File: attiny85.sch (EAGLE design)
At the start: 8 parts, among them U1 TINY85-20-DIP

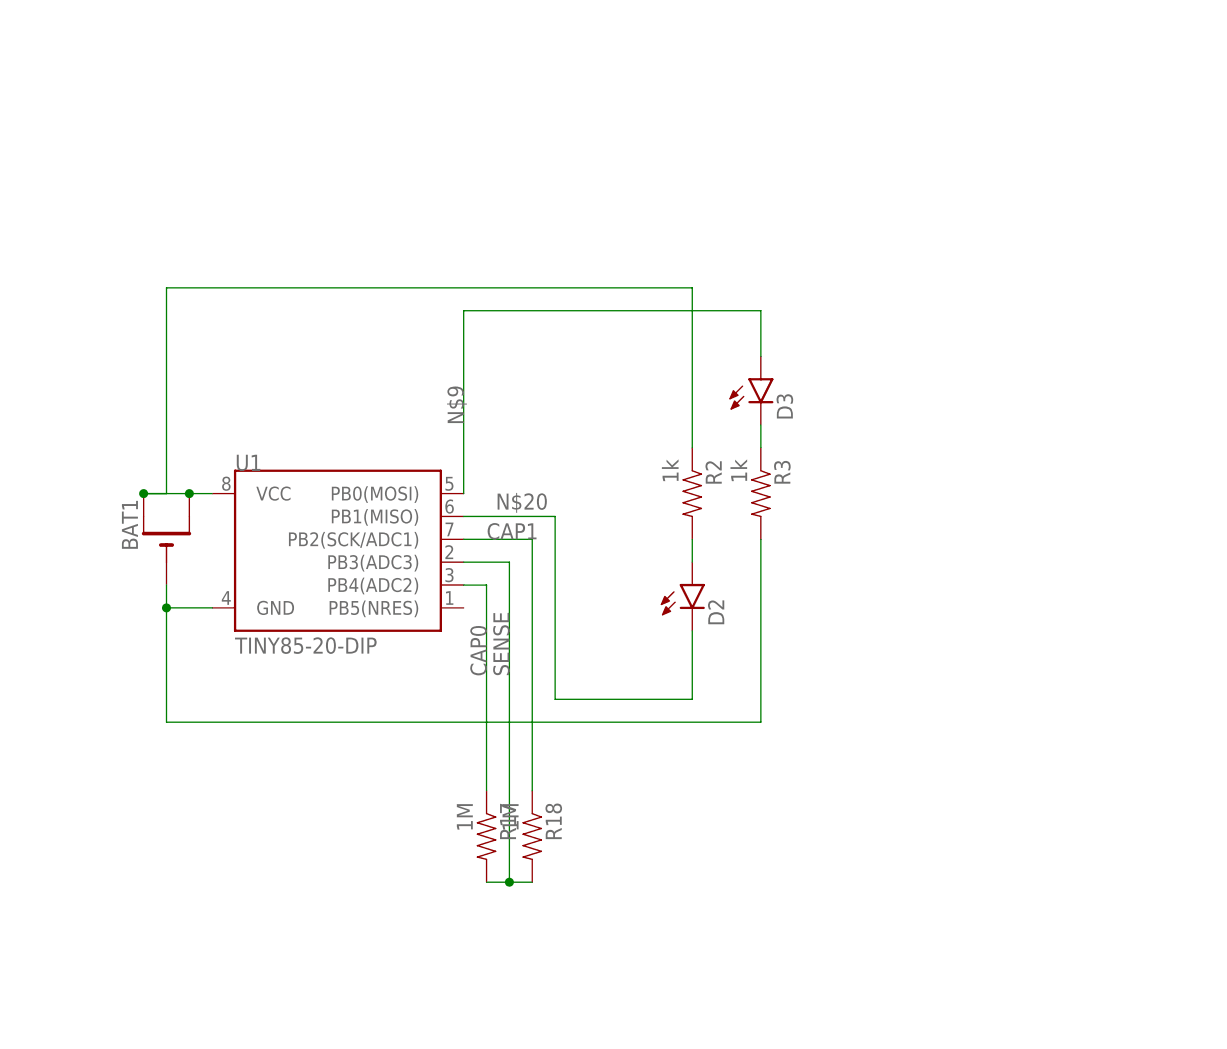
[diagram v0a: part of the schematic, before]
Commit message: Updated schematic and layout for surface mount components
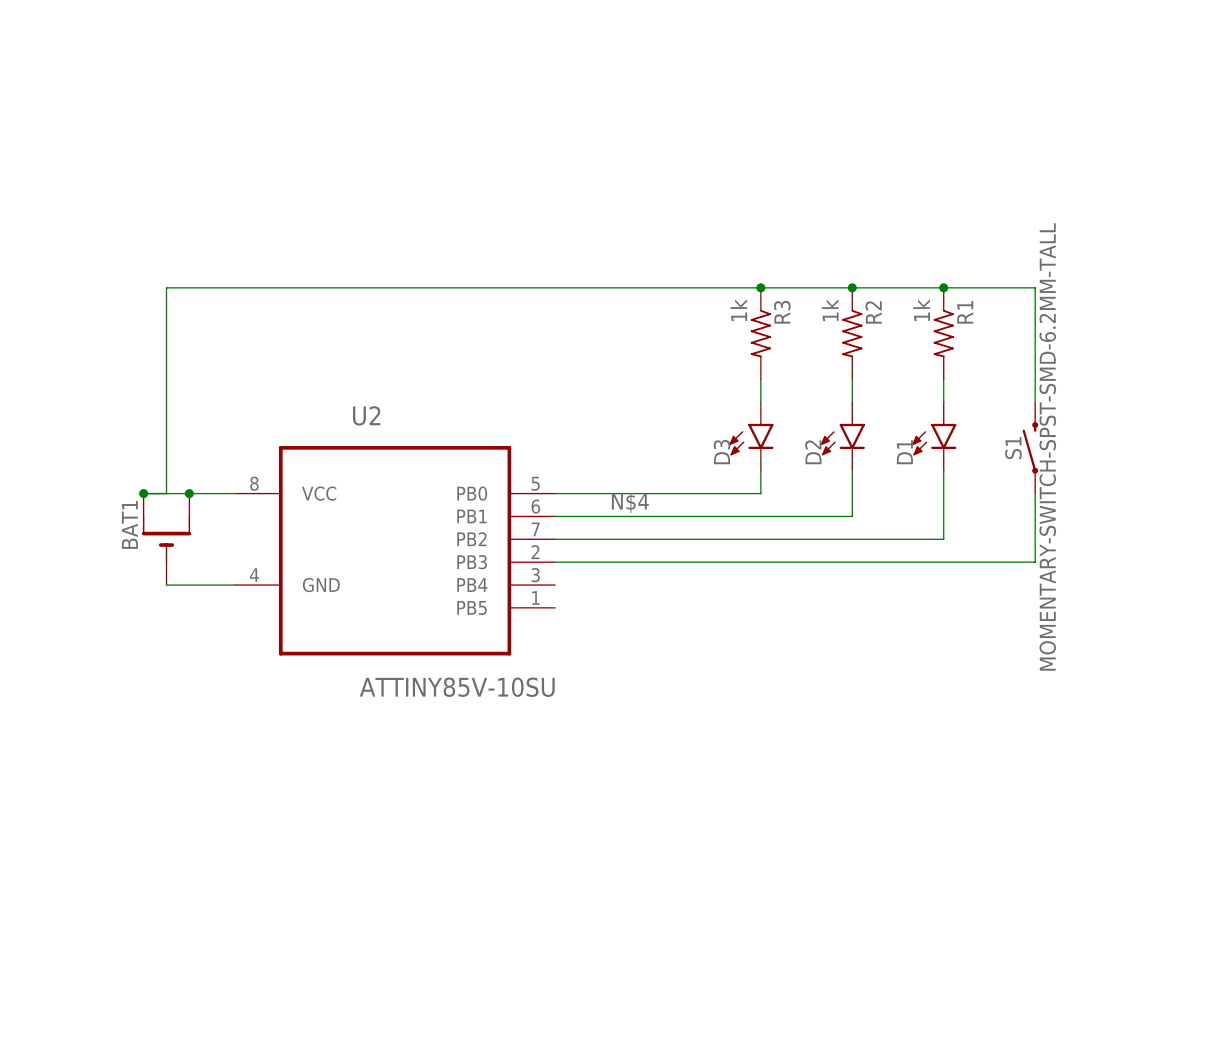
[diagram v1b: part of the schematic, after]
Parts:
- removed R17, R18: 1M, SparkFun-Resistors:1KOHM-1/4W-5%(PTH)
- removed U1: TINY85-20-DIP, SparkFun-DigitalIC:ATTINY45TINY85-20-DIP
- added D1: (no value), SparkFun-LED:LED1206
- added R1: 1k, adafruit:R-US_M1206
- added S1: MOMENTARY-SWITCH-SPST-SMD-6.2MM-TALL, SparkFun-Switches:MOMENTARY-SWITCH-SPST-SMD-6.2MM-TALL
- added U2: ATTINY85V-10SU, Atmel_By_element14_Batch_1-00:ATTINY85V-10SU
- BAT1: device adafruit:CR2032THM -> adafruit:CR2032SMT
- D2, D3: device LED:LED5MM -> SparkFun-LED:LED1206
- R2, R3: device SparkFun-Resistors:1KOHM-1/4W-5%(PTH) -> adafruit:R-US_M1206
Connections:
- removed net CAP0: R17.1, U1.PB4(ADC2)
- removed net CAP1: R18.1, U1.PB2(SCK/ADC1)
- removed net N$20: D2.C, U1.PB1(MISO)
- removed net N$9: D3.A, U1.PB0(MOSI)
- removed net SENSE: R17.2, R18.2, U1.PB3(ADC3)
- new net N$1: D3.A, R3.2
- new net N$4: D2.C, U2.PB1
- new net N$5: D1.A, R1.2
- new net N$6: D1.C, U2.PB2
- new net N$7: S1.1, U2.PB3
- net GND: now also U2.GND; no longer R3.2, U1.GND
- net N$3: now also U2.PB0; no longer R3.1
- net VCC: now also R1.1, R3.1, S1.2, U2.VCC; no longer U1.VCC
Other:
- moved on the sheet: R2, R3
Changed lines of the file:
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@@
 <?xml version="1.0" encoding="utf-8"?>
 <!DOCTYPE eagle SYSTEM "eagle.dtd">
-<eagle version="7.6.0">
+<eagle version="7.7.0">
 <drawing>
 <settings>
@@
 <parts>
 <part name="FRAME1" library="frames" deviceset="TABL_L" device=""/>
-<part name="U1" library="SparkFun-DigitalIC" deviceset="ATTINY45" device="TINY85-20-DIP" value="TINY85-20-DIP"/>
-<part name="R2" library="SparkFun-Resistors" deviceset="1KOHM-1/4W-5%(PTH)" device="" value="1k"/>
-<part name="D2" library="LED" deviceset="LED" device="5MM"/>
-<part name="R3" library="SparkFun-Resistors" deviceset="1KOHM-1/4W-5%(PTH)" device="" value="1k"/>
-<part name="D3" library="LED" deviceset="LED" device="5MM"/>
-<part name="R17" library="SparkFun-Resistors" deviceset="1KOHM-1/4W-5%(PTH)" device="" value="1M"/>
-<part name="R18" library="SparkFun-Resistors" deviceset="1KOHM-1/4W-5%(PTH)" device="" value="1M"/>
-<part name="BAT1" library="adafruit" deviceset="CR2032" device="THM"/>
+<part name="R2" library="adafruit" deviceset="R-US_" device="M1206" value="1k"/>
+<part name="D2" library="SparkFun-LED" deviceset="LED" device="1206"/>
+<part name="R3" library="adafruit" deviceset="R-US_" device="M1206" value="1k"/>
+<part name="D3" library="SparkFun-LED" deviceset="LED" device="1206"/>
+<part name="BAT1" library="adafruit" deviceset="CR2032" device="SMT"/>
+<part name="U2" library="Atmel_By_element14_Batch_1-00" deviceset="ATTINY85V-10SU" device=""/>
+<part name="R1" library="adafruit" deviceset="R-US_" device="M1206" value="1k"/>
+<part name="D1" library="SparkFun-LED" deviceset="LED" device="1206"/>
+<part name="S1" library="SparkFun-Switches" deviceset="MOMENTARY-SWITCH-SPST" device="-SMD-6.2MM-TALL"/>
 </parts>
 <sheets>
@@
 <instance part="FRAME1" gate="G$1" x="0" y="0"/>
 <instance part="FRAME1" gate="G$2" x="299.72" y="0"/>
-<instance part="U1" gate="G$1" x="50.8" y="195.58"/>
-<instance part="R2" gate="G$1" x="88.9" y="203.2" rot="R270"/>
-<instance part="D2" gate="G$1" x="88.9" y="193.04"/>
-<instance part="R3" gate="G$1" x="96.52" y="203.2" rot="R270"/>
-<instance part="D3" gate="G$1" x="96.52" y="215.9"/>
-<instance part="R17" gate="G$1" x="66.04" y="165.1" rot="R270"/>
-<instance part="R18" gate="G$1" x="71.12" y="165.1" rot="R270"/>
+<instance part="R2" gate="G$1" x="106.68" y="220.98" rot="R270"/>
+<instance part="D2" gate="G$1" x="106.68" y="210.82"/>
+<instance part="R3" gate="G$1" x="96.52" y="220.98" rot="R270"/>
+<instance part="D3" gate="G$1" x="96.52" y="210.82"/>
 <instance part="BAT1" gate="G$1" x="30.48" y="198.12" rot="R90"/>
+<instance part="U2" gate="A" x="55.88" y="200.66"/>
+<instance part="R1" gate="G$1" x="116.84" y="220.98" rot="R270"/>
+<instance part="D1" gate="G$1" x="116.84" y="210.82"/>
+<instance part="S1" gate="G$1" x="127" y="208.28" rot="R90"/>
 </instances>
 <busses>
@@
 <pinref part="R2" gate="G$1" pin="2"/>
 <pinref part="D2" gate="G$1" pin="A"/>
-<wire x1="88.9" y1="198.12" x2="88.9" y2="195.58" width="0.1524" layer="91"/>
-</segment>
-</net>
-<net name="CAP1" class="0">
-<segment>
-<pinref part="U1" gate="G$1" pin="PB2(SCK/ADC1)"/>
-<wire x1="63.5" y1="198.12" x2="71.12" y2="198.12" width="0.1524" layer="91"/>
-<wire x1="71.12" y1="198.12" x2="71.12" y2="170.18" width="0.1524" layer="91"/>
-<pinref part="R18" gate="G$1" pin="1"/>
-<label x="66.04" y="198.12" size="1.778" layer="95"/>
-</segment>
-</net>
-<net name="SENSE" class="0">
-<segment>
-<pinref part="R18" gate="G$1" pin="2"/>
-<pinref part="R17" gate="G$1" pin="2"/>
-<wire x1="71.12" y1="160.02" x2="68.58" y2="160.02" width="0.1524" layer="91"/>
-<pinref part="U1" gate="G$1" pin="PB3(ADC3)"/>
-<wire x1="68.58" y1="160.02" x2="66.04" y2="160.02" width="0.1524" layer="91"/>
-<wire x1="63.5" y1="195.58" x2="68.58" y2="195.58" width="0.1524" layer="91"/>
-<wire x1="68.58" y1="195.58" x2="68.58" y2="160.02" width="0.1524" layer="91"/>
-<junction x="68.58" y="160.02"/>
-<label x="68.58" y="182.88" size="1.778" layer="95" rot="R90"/>
-</segment>
-</net>
-<net name="CAP0" class="0">
-<segment>
-<pinref part="U1" gate="G$1" pin="PB4(ADC2)"/>
-<wire x1="63.5" y1="193.04" x2="66.04" y2="193.04" width="0.1524" layer="91"/>
-<wire x1="66.04" y1="193.04" x2="66.04" y2="170.18" width="0.1524" layer="91"/>
-<pinref part="R17" gate="G$1" pin="1"/>
-<label x="66.04" y="182.88" size="1.778" layer="95" rot="R90"/>
-</segment>
-</net>
-<net name="N$3" class="0">
-<segment>
-<pinref part="D3" gate="G$1" pin="C"/>
-<pinref part="R3" gate="G$1" pin="1"/>
-<wire x1="96.52" y1="210.82" x2="96.52" y2="208.28" width="0.1524" layer="91"/>
-</segment>
-</net>
-<net name="N$9" class="0">
-<segment>
-<pinref part="D3" gate="G$1" pin="A"/>
-<wire x1="96.52" y1="218.44" x2="96.52" y2="223.52" width="0.1524" layer="91"/>
-<wire x1="63.5" y1="223.52" x2="96.52" y2="223.52" width="0.1524" layer="91"/>
-<pinref part="U1" gate="G$1" pin="PB0(MOSI)"/>
-<wire x1="63.5" y1="203.2" x2="63.5" y2="223.52" width="0.1524" layer="91"/>
-<label x="63.5" y="210.82" size="1.778" layer="95" rot="R90"/>
-</segment>
-</net>
-<net name="N$20" class="0">
-<segment>
-<pinref part="D2" gate="G$1" pin="C"/>
-<wire x1="88.9" y1="187.96" x2="88.9" y2="180.34" width="0.1524" layer="91"/>
-<pinref part="U1" gate="G$1" pin="PB1(MISO)"/>
-<wire x1="63.5" y1="200.66" x2="73.66" y2="200.66" width="0.1524" layer="91"/>
-<wire x1="73.66" y1="200.66" x2="73.66" y2="180.34" width="0.1524" layer="91"/>
-<wire x1="73.66" y1="180.34" x2="88.9" y2="180.34" width="0.1524" layer="91"/>
-<label x="67.056" y="201.422" size="1.778" layer="95"/>
+<wire x1="106.68" y1="215.9" x2="106.68" y2="213.36" width="0.1524" layer="91"/>
 </segment>
 </net>
@@
 <segment>
 <pinref part="BAT1" gate="G$1" pin="-"/>
-<pinref part="U1" gate="G$1" pin="GND"/>
-<wire x1="35.56" y1="190.5" x2="30.48" y2="190.5" width="0.1524" layer="91"/>
-<junction x="30.48" y="190.5"/>
-<wire x1="30.48" y1="190.5" x2="30.48" y2="193.04" width="0.1524" layer="91"/>
-<wire x1="30.48" y1="190.5" x2="30.48" y2="177.8" width="0.1524" layer="91"/>
-<wire x1="30.48" y1="177.8" x2="96.52" y2="177.8" width="0.1524" layer="91"/>
-<pinref part="R3" gate="G$1" pin="2"/>
-<wire x1="96.52" y1="198.12" x2="96.52" y2="177.8" width="0.1524" layer="91"/>
+<pinref part="U2" gate="A" pin="GND"/>
+<wire x1="38.1" y1="193.04" x2="30.48" y2="193.04" width="0.1524" layer="91"/>
 </segment>
 </net>
@@
 <segment>
 <pinref part="R2" gate="G$1" pin="1"/>
-<wire x1="88.9" y1="226.06" x2="88.9" y2="208.28" width="0.1524" layer="91"/>
-<pinref part="U1" gate="G$1" pin="VCC"/>
-<wire x1="35.56" y1="203.2" x2="33.02" y2="203.2" width="0.1524" layer="91"/>
 <pinref part="BAT1" gate="G$1" pin="+"/>
 <junction x="27.94" y="203.2"/>
@@
 <wire x1="27.94" y1="203.2" x2="30.48" y2="203.2" width="0.1524" layer="91"/>
 <wire x1="30.48" y1="203.2" x2="30.48" y2="226.06" width="0.1524" layer="91"/>
-<wire x1="30.48" y1="226.06" x2="88.9" y2="226.06" width="0.1524" layer="91"/>
+<wire x1="30.48" y1="226.06" x2="96.52" y2="226.06" width="0.1524" layer="91"/>
 <pinref part="BAT1" gate="G$1" pin="+1"/>
+<pinref part="U2" gate="A" pin="VCC"/>
+<wire x1="96.52" y1="226.06" x2="106.68" y2="226.06" width="0.1524" layer="91"/>
+<wire x1="38.1" y1="203.2" x2="33.02" y2="203.2" width="0.1524" layer="91"/>
 <junction x="33.02" y="203.2"/>
-</segment>
-</net>
+<pinref part="R3" gate="G$1" pin="1"/>
+<junction x="96.52" y="226.06"/>
+<pinref part="R1" gate="G$1" pin="1"/>
+<wire x1="106.68" y1="226.06" x2="116.84" y2="226.06" width="0.1524" layer="91"/>
+<junction x="106.68" y="226.06"/>
+<pinref part="S1" gate="G$1" pin="2"/>
+<wire x1="116.84" y1="226.06" x2="127" y2="226.06" width="0.1524" layer="91"/>
+<wire x1="127" y1="226.06" x2="127" y2="213.36" width="0.1524" layer="91"/>
+<junction x="116.84" y="226.06"/>
+</segment>
+</net>
+<net name="N$1" class="0">
+<segment>
+<pinref part="R3" gate="G$1" pin="2"/>
+<pinref part="D3" gate="G$1" pin="A"/>
+<wire x1="96.52" y1="215.9" x2="96.52" y2="213.36" width="0.1524" layer="91"/>
+</segment>
+</net>
+<net name="N$3" class="0">
+<segment>
+<pinref part="D3" gate="G$1" pin="C"/>
+<pinref part="U2" gate="A" pin="PB0"/>
+<wire x1="96.52" y1="205.74" x2="96.52" y2="203.2" width="0.1524" layer="91"/>
+<wire x1="96.52" y1="203.2" x2="73.66" y2="203.2" width="0.1524" layer="91"/>
+</segment>
+</net>
+<net name="N$4" class="0">
+<segment>
+<wire x1="73.66" y1="200.66" x2="106.68" y2="200.66" width="0.1524" layer="91"/>
+<pinref part="U2" gate="A" pin="PB1"/>
+<label x="79.756" y="201.422" size="1.778" layer="95"/>
+<pinref part="D2" gate="G$1" pin="C"/>
+<wire x1="106.68" y1="205.74" x2="106.68" y2="200.66" width="0.1524" layer="91"/>
+</segment>
+</net>
+<net name="N$5" class="0">
+<segment>
+<pinref part="R1" gate="G$1" pin="2"/>
+<pinref part="D1" gate="G$1" pin="A"/>
+<wire x1="116.84" y1="215.9" x2="116.84" y2="213.36" width="0.1524" layer="91"/>
+</segment>
+</net>
+<net name="N$6" class="0">
+<segment>
+<pinref part="D1" gate="G$1" pin="C"/>
+<pinref part="U2" gate="A" pin="PB2"/>
+<wire x1="116.84" y1="205.74" x2="116.84" y2="198.12" width="0.1524" layer="91"/>
+<wire x1="116.84" y1="198.12" x2="73.66" y2="198.12" width="0.1524" layer="91"/>
+</segment>
+</net>
+<net name="N$7" class="0">
+<segment>
+<pinref part="S1" gate="G$1" pin="1"/>
+<pinref part="U2" gate="A" pin="PB3"/>
+<wire x1="127" y1="203.2" x2="127" y2="195.58" width="0.1524" layer="91"/>
+<wire x1="127" y1="195.58" x2="73.66" y2="195.58" width="0.1524" layer="91"/>
+</segment>
+</net>
